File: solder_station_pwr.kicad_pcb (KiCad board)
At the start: 2 copper layers, 100.2 x 69.2 mm, 47 parts, among them J1 PWR_MAIN_LINE, J2 FB, J3 Conn_01x04, J5 DESOLDER, J6 Conn_01x03, Q3 2SD669, T1 RingTrafo_40U, T2 220V-7V5, U1 TLC555, U2 L7805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

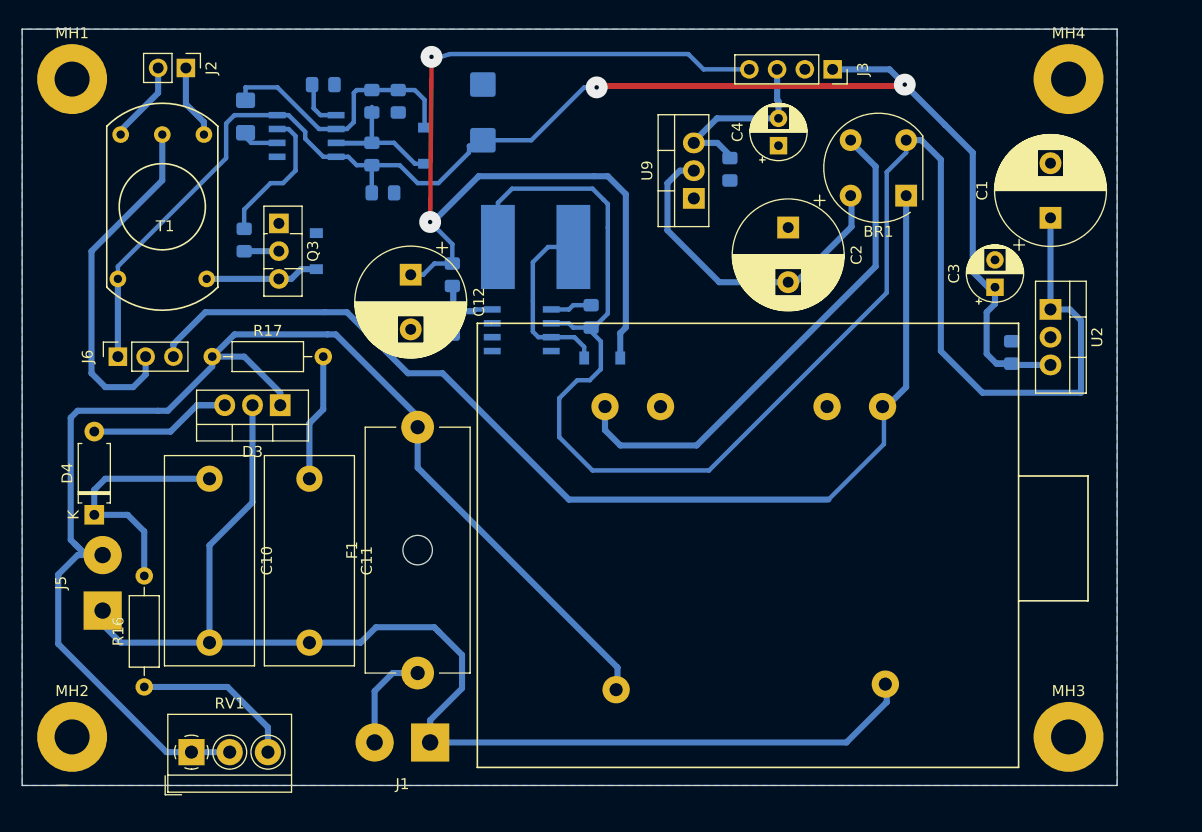
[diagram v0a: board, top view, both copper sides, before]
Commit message: add darligton stage instead of simple transitor
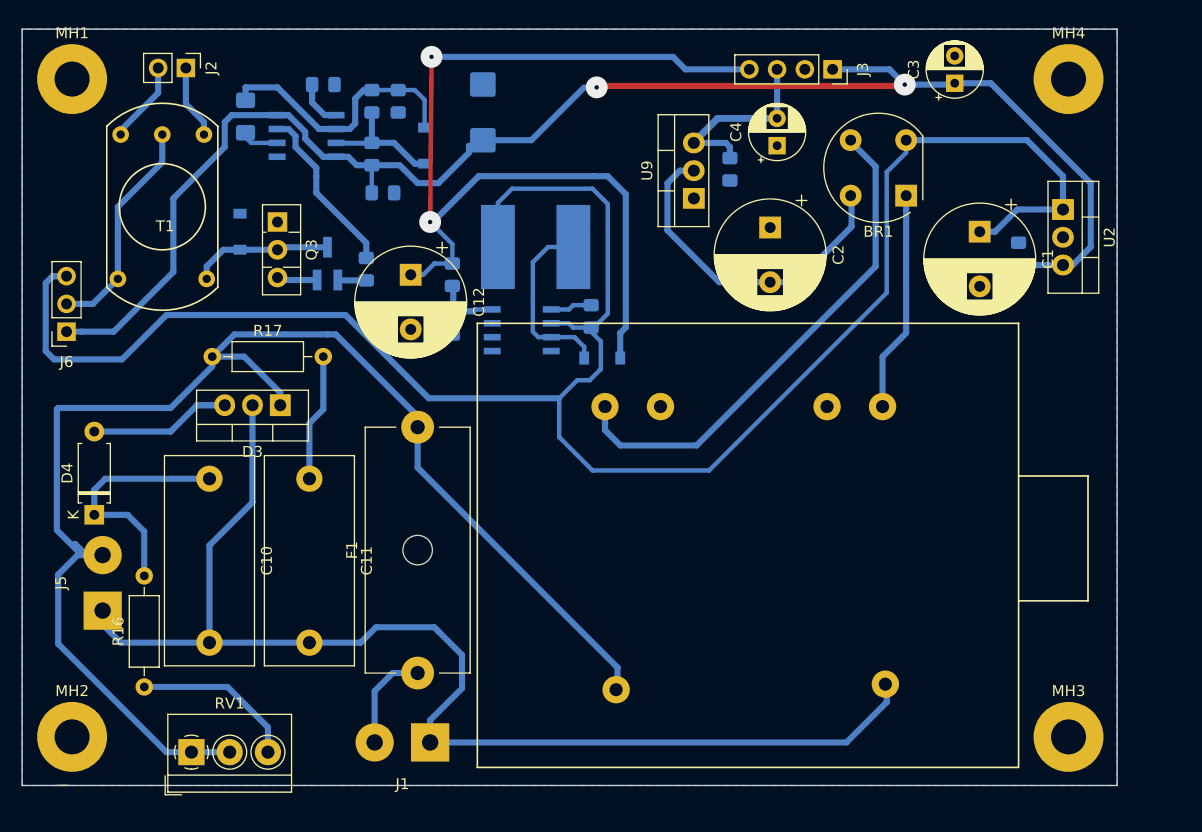
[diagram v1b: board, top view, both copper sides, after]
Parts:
- added Q1: 2N7002, Package_TO_SOT_SMD:SOT-23_Handsoldering, B.Cu at (50.0, 39.5)
- C14: value 10n -> 4n7
- moved C3 19.0 mm to (107.4, 23.0)
- moved R3 11.5 mm to (53.6, 40.0)
- moved U2 9.22 mm to (117.3, 34.5)
- moved C5 9.04 mm to (113.3, 38.6)
- moved D2 7.21 mm to (42.0, 36.6)
- moved C1 6.60 mm to (109.7, 36.6), turned to 270 degrees
- moved J6 5.23 mm to (26.2, 45.7), turned to 180 degrees
- moved C2 1.65 mm to (90.6, 36.2)
- moved Q3 0.18 mm to (45.5, 35.7)
- moved C4 0.13 mm to (91.2, 28.7)
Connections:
- BR1 pad 1: /7V5P -> Net-(BR1-Pad1)
- J6 pad 3: /7V5P -> /UNR_5V
- Q3 pad 2: Net-(Q3-Pad2) -> Net-(D2-Pad1)
- Q3 pad 3: Net-(D2-Pad1) -> Net-(Q1-Pad2)
- R3 pad 1: Net-(Q3-Pad2) -> Net-(Q1-Pad1)
- T1 pad 1: +5V -> Net-(J6-Pad2)
- T2 pad 3: /7V5P -> Net-(BR1-Pad1)
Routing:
- net /7V5P: track 100.2 -> 0.00 mm
- net /UNR_5V: track 153.2 -> 187.7 mm
- net Net-(BR1-Pad1): track 0.00 -> 20.2 mm
- net Net-(J6-Pad2): track 32.1 -> 20.5 mm
- net Net-(C14-Pad1): track 25.4 -> 35.0 mm
- net -5V: track 17.3 -> 26.3 mm
- net /240AV+: track 128.5 -> 133.9 mm
- net Net-(Q1-Pad2): track 0.00 -> 3.72 mm
- net Net-(D1-Pad2): track 19.2 -> 15.7 mm
- net Net-(Q3-Pad2): track 3.18 -> 0.00 mm
- net Net-(R3-Pad2): track 13.1 -> 15.8 mm
- net Net-(Q1-Pad1): track 0.00 -> 2.62 mm
- net Net-(D2-Pad1): track 10.4 -> 12.9 mm

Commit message: remove ne555, using the atmega pwm OC0B to control the transistor
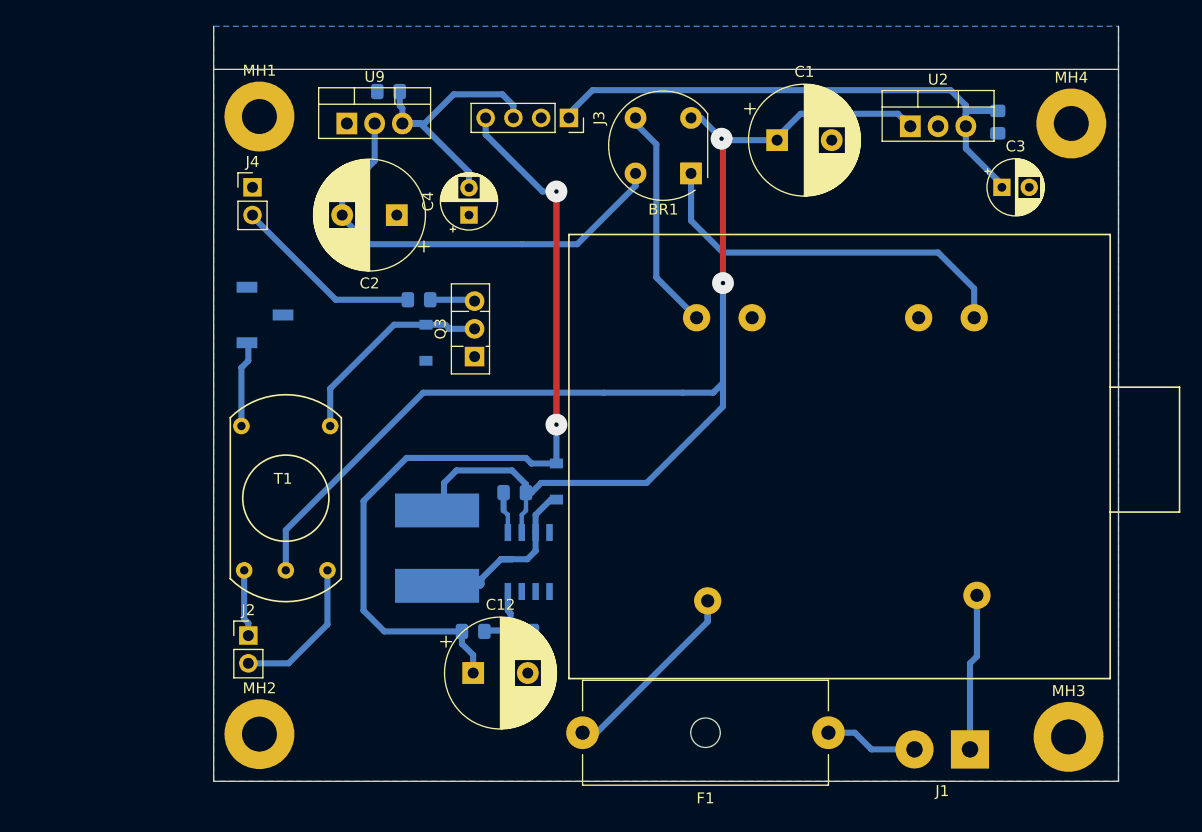
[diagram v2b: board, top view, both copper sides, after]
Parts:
- removed C10, C11: 0.33u/400V, Capacitor_THT:C_Rect_L19.0mm_W8.0mm_P15.00mm_MKS4
- removed C14: 4n7, Capacitor_SMD:C_0805_2012Metric_Pad1.15x1.40mm_HandSolder
- removed C15: 10n, Capacitor_SMD:C_0805_2012Metric_Pad1.15x1.40mm_HandSolder
- removed C16: 100n, Capacitor_SMD:C_0805_2012Metric_Pad1.15x1.40mm_HandSolder
- removed C17: 10u, Capacitor_Tantalum_SMD:CP_EIA-6032-15_Kemet-U_Pad2.25x2.35mm_HandSolder
- removed D1: SD103BW, Diode_SMD:D_SOD-123
- removed D3: TLC381, Package_TO_SOT_THT:TO-220-3_Vertical
- removed D4: ER900, Diode_THT:D_A-405_P7.62mm_Horizontal
- removed J5: DESOLDER, Connector_Wire:SolderWirePad_1x02_P5.08mm_Drill1.5mm
- removed Q1: 2N7002, Package_TO_SOT_SMD:SOT-23_Handsoldering
- removed R1, R2: 1k, Resistor_SMD:R_0805_2012Metric_Pad1.15x1.40mm_HandSolder
- removed R16: 10k, Resistor_THT:R_Axial_DIN0207_L6.3mm_D2.5mm_P10.16mm_Horizontal
- removed R17: 330k, Resistor_THT:R_Axial_DIN0207_L6.3mm_D2.5mm_P10.16mm_Horizontal
- removed R4: 0, Resistor_SMD:R_1206_3216Metric_Pad1.42x1.75mm_HandSolder
- removed RV1: 200k, TerminalBlock_4Ucon:TerminalBlock_4Ucon_1x03_P3.50mm_Horizontal
- removed U1: TLC555, Package_SO:SOIC-8_3.9x4.9mm_P1.27mm
- added J4: FB_IN, Connector_PinHeader_2.54mm:PinHeader_1x02_P2.54mm_Vertical, F.Cu at (43.2, 32.5)
- J2: value FB -> FB_OUT
- J6: footprint Connector_PinSocket_2.54mm:PinSocket_1x03_P2.54mm_Vertical -> Connector_PinSocket_2.54mm:PinSocket_1x03_P2.54mm_Vertical_SMD_Pin1Left; moved to B.Cu
- moved J2 52.3 mm to (42.8, 73.5), turned to 0 degrees
- moved J1 49.4 mm to (108.8, 83.9)
- moved F1 38.0 mm to (95.9, 82.4), turned to 180 degrees
- moved C12 36.9 mm to (63.4, 77.0), turned to 0 degrees
- moved C2 34.2 mm to (56.4, 35.1), turned to 180 degrees
- moved R24 32.7 mm to (63.4, 73.2), turned to 0 degrees
- moved U9 32.5 mm to (51.8, 26.7), turned to 0 degrees
- moved C6 32.0 mm to (55.6, 23.7), turned to 0 degrees
- moved L1 29.0 mm to (60.1, 65.5), turned to 270 degrees
- moved T1 29.0 mm to (46.2, 61.0), turned to 180 degrees
- moved C4 28.9 mm to (63.0, 35.1)
- moved R25 28.9 mm to (67.8, 73.2), turned to 0 degrees
- moved J3 24.5 mm to (72.1, 26.2)
- moved Q3 21.8 mm to (63.5, 48.0), turned to 90 degrees
- moved U8 21.2 mm to (68.5, 66.8), turned to 270 degrees
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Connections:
- J2 pad 1: /FB2 -> /FB1
- J2 pad 2: /FB1 -> /FB2
- J6 pad 1: +5V -> Net-(J6-Pad1)
- J6 pad 2: Net-(J6-Pad2) -> GND
- J6 pad 3: /UNR_5V -> (no net)
- Q3 pad 3: Net-(Q1-Pad2) -> Net-(Q3-Pad3)
- R3 pad 1: Net-(Q1-Pad1) -> Net-(Q3-Pad3)
- T1 pad 1: Net-(J6-Pad2) -> Net-(D2-Pad1)
- T1 pad 2: Net-(D2-Pad1) -> Net-(J6-Pad1)
- T1 pad 3: /FB1 -> /FB2
- T1 pad 4: Net-(J6-Pad2) -> /UNR_5V
- T1 pad 5: /FB2 -> /FB1
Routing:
- net /240AV+: track 133.9 -> 19.2 mm
- net /240AV-: track 113.8 -> 14.4 mm
- net +5V: track 140.8 -> 53.1 mm, vias 2 -> 0
- net /UNR_5V: track 187.7 -> 133.2 mm, vias 0 -> 2
- net Net-(C14-Pad1): track 35.0 -> 0.00 mm
- net Net-(BR1-Pad3): track 49.0 -> 20.6 mm
- net Net-(C10-Pad1): track 22.5 -> 0.00 mm
- net Net-(J6-Pad2): track 20.5 -> 0.00 mm
- net Net-(D1-Pad2): track 15.7 -> 0.00 mm
- net Net-(D3-Pad3): track 15.5 -> 0.00 mm
- net Net-(BR1-Pad1): track 20.2 -> 35.5 mm
- net Net-(R16-Pad1): track 15.1 -> 0.00 mm
- net Net-(C11-Pad1): track 11.7 -> 0.00 mm
- net +36V: track 89.1 -> 78.6 mm
- net Net-(BR1-Pad4): track 31.0 -> 41.0 mm
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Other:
- board size 100.2 x 69.2 mm -> 82.8 x 69.1 mm

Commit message: Add power suppply has now just 2 differents 5 volt and a -5 volt
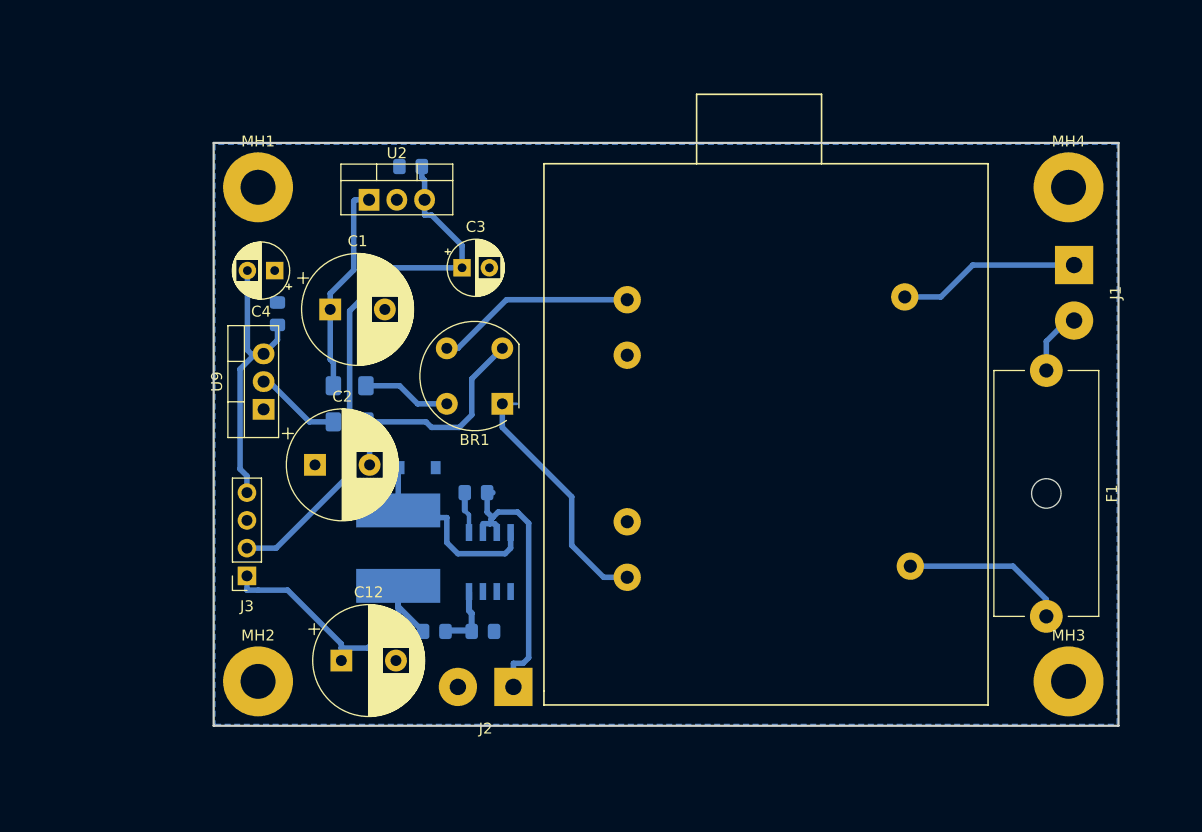
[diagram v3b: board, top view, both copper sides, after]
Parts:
- removed D2: SD103BW, Diode_SMD:D_SOD-123
- removed J4: FB_IN, Connector_PinHeader_2.54mm:PinHeader_1x02_P2.54mm_Vertical
- removed J6: Conn_01x03, Connector_PinSocket_2.54mm:PinSocket_1x03_P2.54mm_Vertical_SMD_Pin1Left
- removed Q3: 2SD669, Package_TO_SOT_THT:TO-126-3_Vertical
- removed R3: 1k, Resistor_SMD:R_0805_2012Metric_Pad1.15x1.40mm_HandSolder
- removed T1: RingTrafo_40U, custom:Transformer_toroid_v_18mm
- added R1: 0, Resistor_SMD:R_1206_3216Metric_Pad1.42x1.75mm_HandSolder, B.Cu at (52.1, 54.0)
- added R2: 0, Resistor_SMD:R_1206_3216Metric_Pad1.42x1.75mm_HandSolder, B.Cu at (52.1, 50.7)
- J2: value FB_OUT -> PWR_HV; footprint Connector_PinHeader_2.54mm:PinHeader_1x02_P2.54mm_Vertical -> Connector_Wire:SolderWirePad_1x02_P5.08mm_Drill1.5mm
- J3: value Conn_01x04 -> PWR_LV
- R24: value 1M -> 560k
- R25: value 6k8 -> 22k
- moved C5 53.9 mm to (57.6, 30.6), turned to 180 degrees
- moved J3 51.2 mm to (42.7, 68.1), turned to 180 degrees
- moved U2 50.0 mm to (53.8, 33.7)
- moved C3 49.9 mm to (62.4, 39.9)
- moved J1 45.3 mm to (118.4, 39.6), turned to 270 degrees
- moved C1 43.7 mm to (50.3, 43.7)
- moved F1 38.7 mm to (115.8, 49.3), turned to 270 degrees
- moved BR1 27.3 mm to (66.0, 52.3)
- moved U9 27.2 mm to (44.2, 52.8), turned to 90 degrees
- moved J2 24.7 mm to (67.1, 78.2), turned to 180 degrees
- moved C2 24.1 mm to (48.9, 57.9), turned to 0 degrees
- moved C6 22.7 mm to (45.5, 44.1), turned to 270 degrees
- moved C4 18.5 mm to (45.2, 40.1), turned to 180 degrees
- moved D6 12.8 mm to (58.3, 58.2), turned to 0 degrees
- moved C12 12.1 mm to (51.3, 75.8)
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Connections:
- BR1 pad 2: /UNR_5V -> Net-(BR1-Pad2)
- C1 pad 1: /UNR_5V -> Net-(BR1-Pad4)
- C12 pad 1: +36V -> +5VA
- C2 pad 2: Net-(BR1-Pad4) -> Net-(BR1-Pad2)
- D6 pad 1: +36V -> Net-(D6-Pad1)
- D6 pad 2: Net-(D6-Pad2) -> GND
- J2 pad 1: /FB1 -> +12V
- J2 pad 2: /FB2 -> GND
- J3 pad 1: +5V -> +5VA
- J3 pad 2: GND -> +5V
- J3 pad 3: -5V -> GND
- J3 pad 4: +36V -> -5V
- L1 pad 1: /UNR_5V -> Net-(D6-Pad1)
- L1 pad 2: Net-(D6-Pad2) -> +5VA
- R22 pad 1: /UNR_5V -> +12V
- R24 pad 1: +36V -> +5VA
- T2 pad 3: Net-(BR1-Pad1) -> Net-(BR1-Pad3)
- T2 pad 6: Net-(BR1-Pad3) -> Net-(BR1-Pad1)
- U2 pad 1: /UNR_5V -> Net-(BR1-Pad4)
- U8 pad 2: /UNR_5V -> +12V
- U8 pad 3: Net-(D6-Pad2) -> +12V
- U8 pad 4: GND -> Net-(D6-Pad1)
- U9 pad 2: Net-(BR1-Pad4) -> Net-(BR1-Pad2)
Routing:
- net /UNR_5V: track 133.2 -> 0.00 mm, vias 2 -> 0
- net +36V: track 78.6 -> 0.00 mm, vias 2 -> 0
- net Net-(BR1-Pad2): track 0.00 -> 29.6 mm
- net +12V: track 0.00 -> 28.6 mm
- net +5VA: track 0.00 -> 27.9 mm
- net Net-(D6-Pad2): track 20.2 -> 0.00 mm
- net Net-(D2-Pad1): track 19.2 -> 0.00 mm
- net Net-(D6-Pad1): track 0.00 -> 18.9 mm
- net Net-(J4-Pad2): track 17.5 -> 0.00 mm
- net /FB2: track 13.7 -> 0.00 mm
- net Net-(BR1-Pad4): track 41.0 -> 27.4 mm
- net Net-(BR1-Pad1): track 35.5 -> 23.2 mm
- net Net-(J6-Pad1): track 7.94 -> 0.00 mm
- net /FB1: track 6.13 -> 0.00 mm
- net Net-(Q3-Pad3): track 4.11 -> 0.00 mm
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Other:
- board size 82.8 x 69.1 mm -> 82.8 x 53.3 mm
- net class signal: trace_width 0.25 -> 0.508
